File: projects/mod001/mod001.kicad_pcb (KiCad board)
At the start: 2 copper layers, 90.2 x 59.7 mm, 14 parts, among them U1 LD1117S33TR, U2 SFC_MaskRom_32pin_SOCKET, U3 74LVC245, U4 74LVC245, U5 74LVC245, U6 SST39VF1681_1682

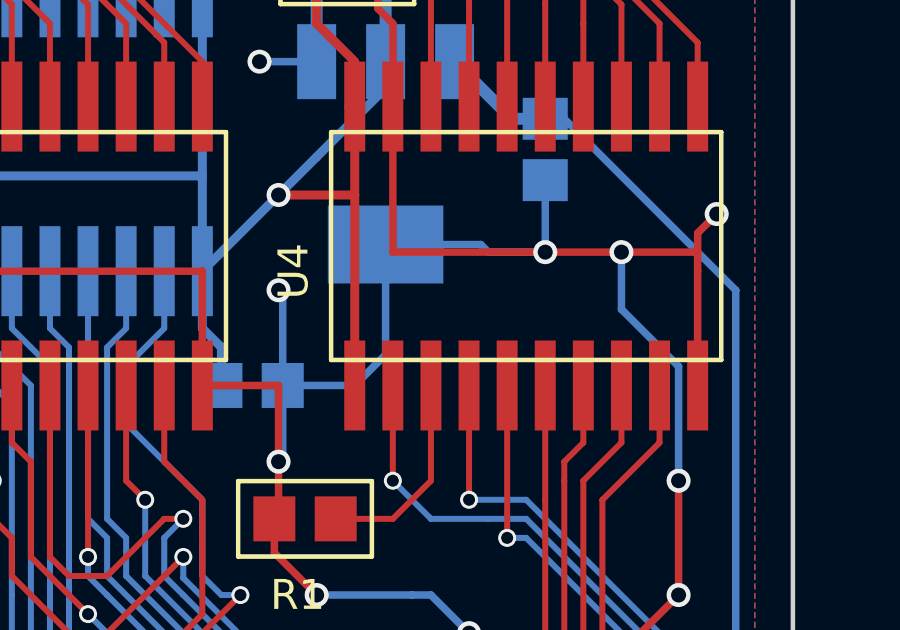
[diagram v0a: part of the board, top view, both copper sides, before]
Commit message: Fixed mod001 (making pin 4 of U1 unconnected).
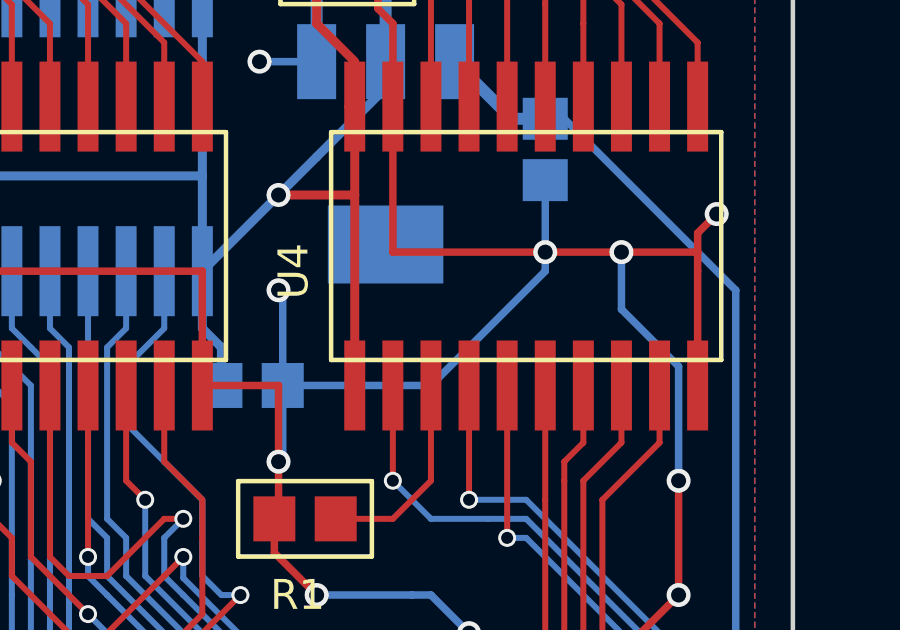
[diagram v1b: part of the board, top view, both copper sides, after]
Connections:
- U1 pad 4: GND_ -> (no net)
- U3 pad 18: Net-(U3-Pad18) -> (no net)
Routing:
- net GND_: track 632.1 -> 630.2 mm
